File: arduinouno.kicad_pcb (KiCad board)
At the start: 2 copper layers, 68.6 x 53.3 mm, 106 parts, among them J1 M20-7820842, J2 M20-7820646, J3 M20-7820842, J4 M20-7821046, J5 67997-106HLF, J6 67997-106HLF, J7 10118193-0001LF, J8 PAD_WITH_HOLE_4mmx1.5mm, J9 PAD_WITH_HOLE_4mmx1.5mm, SW1 1825910-6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

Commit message: improved layout, almost complete
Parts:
- moved C29 0.70 mm to (124.3, 84.7)
- moved SW1 0.45 mm to (164.5, 75.8)
- moved C3 0.40 mm to (124.0, 81.1)
- moved R18 0.40 mm to (168.0, 84.2)
- moved C4 0.40 mm to (121.8, 81.1)
- moved U6 0.40 mm to (167.3, 88.2)
- moved C32 0.35 mm to (165.9, 84.2)
- moved FB1 0.35 mm to (121.8, 84.7)
- moved R20 0.35 mm to (168.0, 80.9)
- moved U7 0.20 mm to (123.6, 88.6)
- moved R24 0.16 mm to (166.1, 80.9)
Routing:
- net +5V_3V3: track 117.5 -> 96.2 mm, vias 12 -> 16
- net GND: track 165.6 -> 144.6 mm, vias 39 -> 45
- net +5V: track 42.2 -> 21.4 mm
- net +3V3: track 12.9 -> 0.07 mm
- net /+5_3V3_328P_VCC: track 18.8 -> 7.40 mm
- net /+5V_USB: track 10.6 -> 2.89 mm
- net /+5_3V3_328P_AVCC: track 6.97 -> 1.92 mm
- net +AREF: track 89.1 -> 92.1 mm, vias 2 -> 3
- net /16U2_TXD: track 50.6 -> 48.7 mm
- net /+5_3V3_16U2: track 26.6 -> 28.4 mm
- net /16U2_RXD: track 48.2 -> 46.6 mm
- net /IO0: track 35.5 -> 37.1 mm
- net /IO1: track 33.5 -> 35.2 mm
- net /MISO: track 84.5 -> 85.9 mm
- net /328P_AUTORESETn: track 36.4 -> 35.1 mm
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- added copper zone on F.Cu, net +3V3
- added copper zone on F.Cu, net +5V
- added copper zone on F.Cu, net +5V_3V3
- added copper zone on F.Cu, net /+5V_USB
- added copper zone on F.Cu, net /+5_3V3_328P_AVCC
- added copper zone on B.Cu, net /+5_3V3_328P_VCC
- added copper zone on F.Cu, net /+5_3V3_328P_VCC
- added copper zone on F.Cu, net GND
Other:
- net class Power: trace_width 0.4 -> 0.6

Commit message: completed layout, drc ok
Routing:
- net GND: track 144.6 -> 82.0 mm, vias 45 -> 58
- net /SCK: track 85.8 -> 86.6 mm

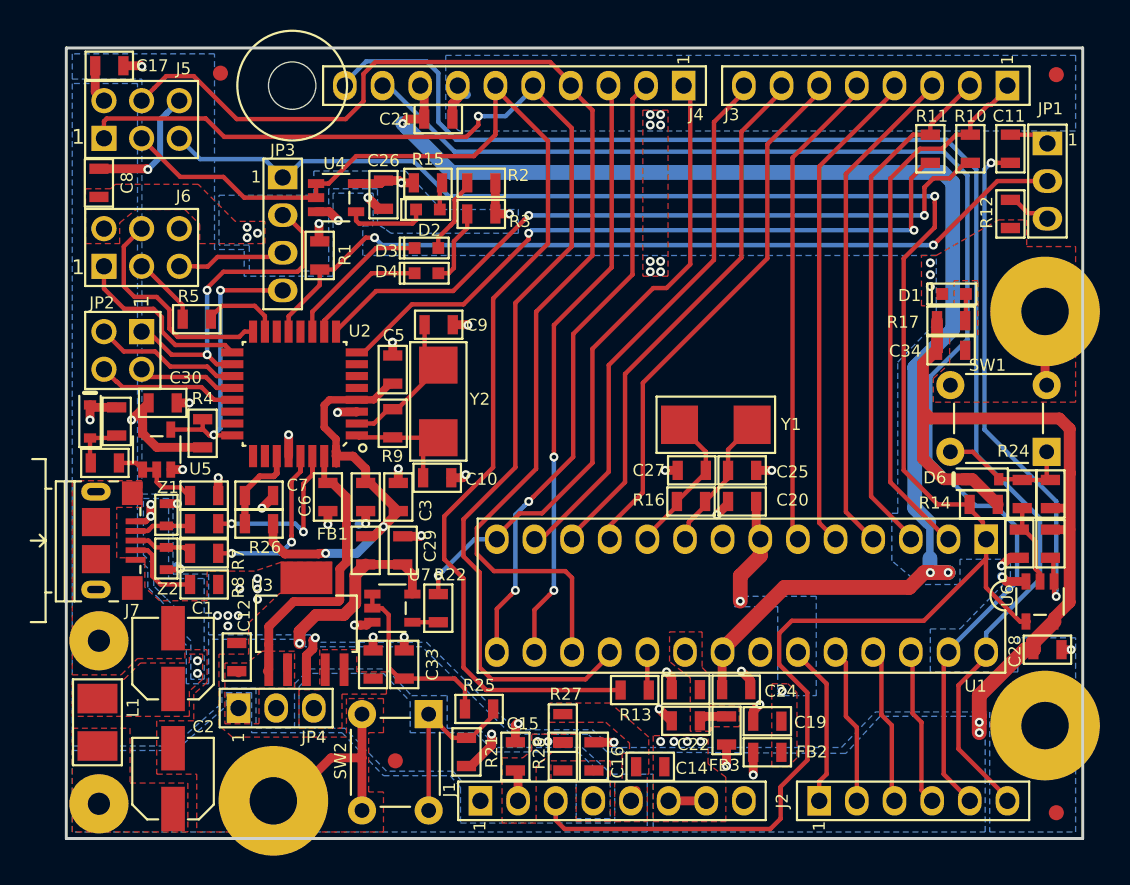
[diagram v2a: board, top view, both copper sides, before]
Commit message: updated silkscreen
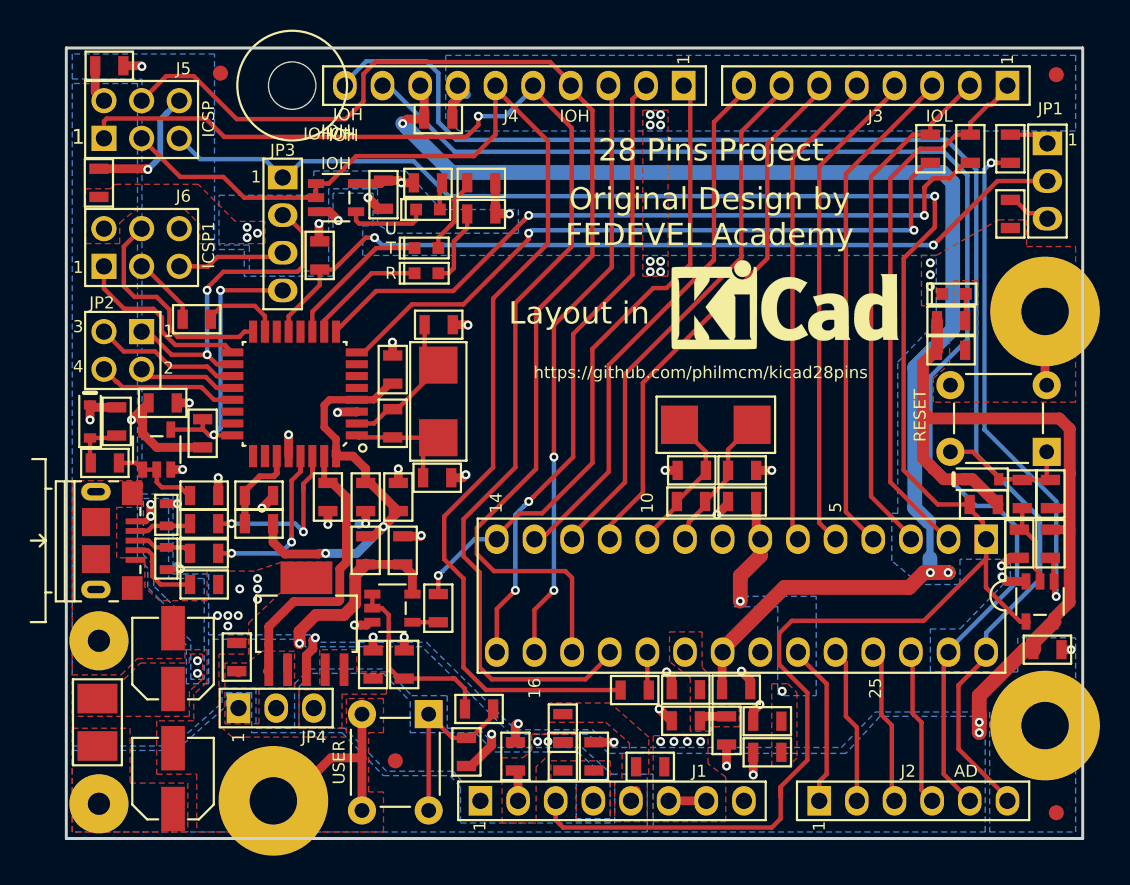
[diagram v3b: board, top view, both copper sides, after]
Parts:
- added REF***: KiCad-Logo_6mm_SilkScreen, Symbols:KiCad-Logo_6mm_SilkScreen, F.Cu at (150.1, 68.1)
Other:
- board text added: "(c) 2015 FEDEVEL www.fedevel.com www.28pins.com KiCad adaptation by Phil McMillan https://github.com/philmcm/kicad28pins Thank you Robert Feranec!"
- board text added: "+"
- board text added: "+3.3V"
- board text added: "+5V"
- board text added: "+5V INPUT POWER (OPTIONAL)"
- board text added: "-"
- board text added: "0 RX (IN)"
- board text added: "1 TX (OUT)"
- board text added: "10"
- board text added: "11"
- board text added: "12"
- board text added: "13"
- board text added: "14"
- board text added: "16"
- board text added: "2"
- board text added: "25"
- board text added: "28 Pins Project"
- board text added: "3"
- board text added: "3.3/5V"
- board text added: "3.3V"
- board text added: "4"
- board text added: "5"
- board text added: "5V"
- board text added: "5V/3V3"
- board text added: "6"
- board text added: "7"
- board text added: "8"
- board text added: "9"
- board text added: "A0"
- board text added: "A1"
- board text added: "A2"
- board text added: "A3"
- board text added: "A4"
- board text added: "A5"
- board text added: "AD"
- board text added: "AD4/SDA"
- board text added: "AD5/SCL"
- board text added: "AR/DF"
- board text added: "AREF"
- board text added: "BOARD VARIANT"
- board text added: "CUSTOM"
- board text added: "FIXED 5V"
- board text added: "GND"
- board text added: "ICSP"
- board text added: "ICSP1"
- board text added: "IO"
- board text added: "IOH"
- board text added: "IOL"
- board text added: "Layout in"
- board text added: "NC"
- board text added: "Original Design by FEDEVEL Academy"
- board text added: "R"
- board text added: "RESET"
- board text added: "T"
- board text added: "U"
- board text added: "USER"
- board text added: "dW/PROG/ISP"
- board text added: "https://github.com/philmcm/kicad28pins"
